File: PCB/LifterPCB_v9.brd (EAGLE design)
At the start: 64.9 x 58.5 mm, 8 parts

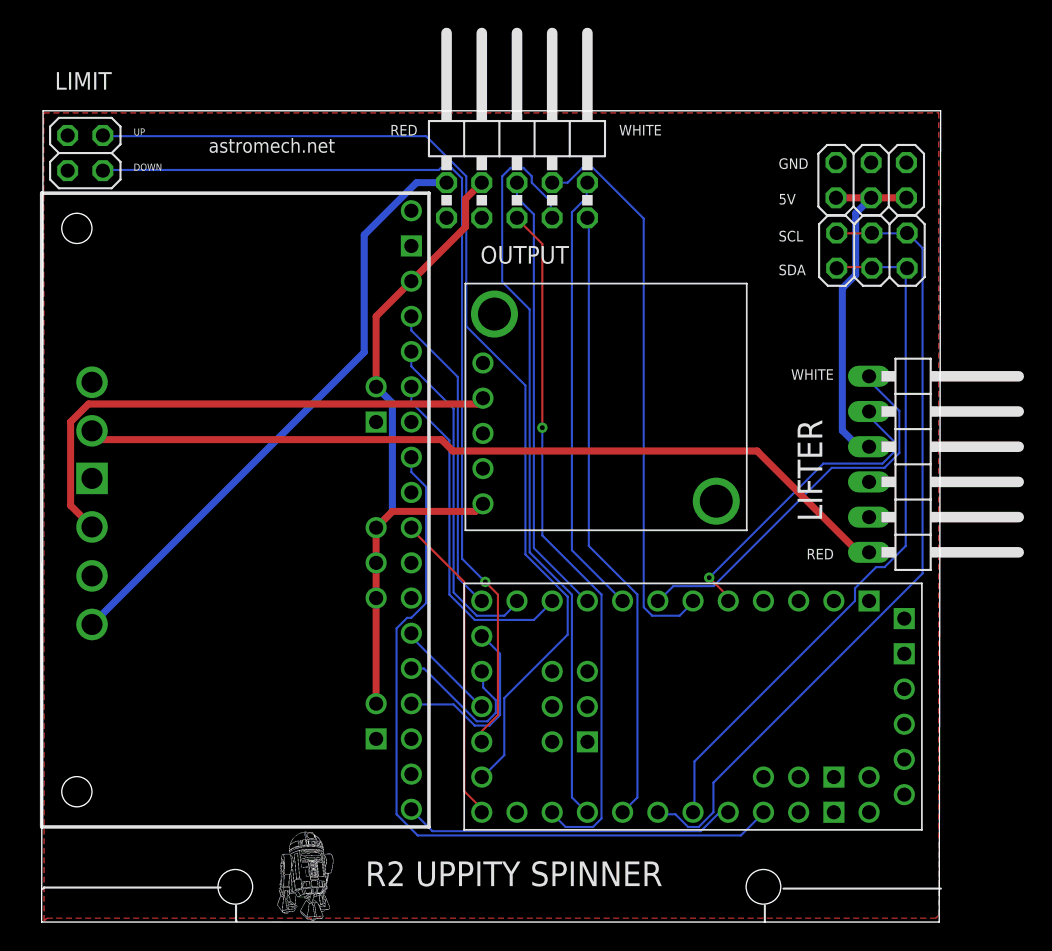
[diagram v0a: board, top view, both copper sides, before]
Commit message: Latest version of Eagle board files plus Eagle v9 version
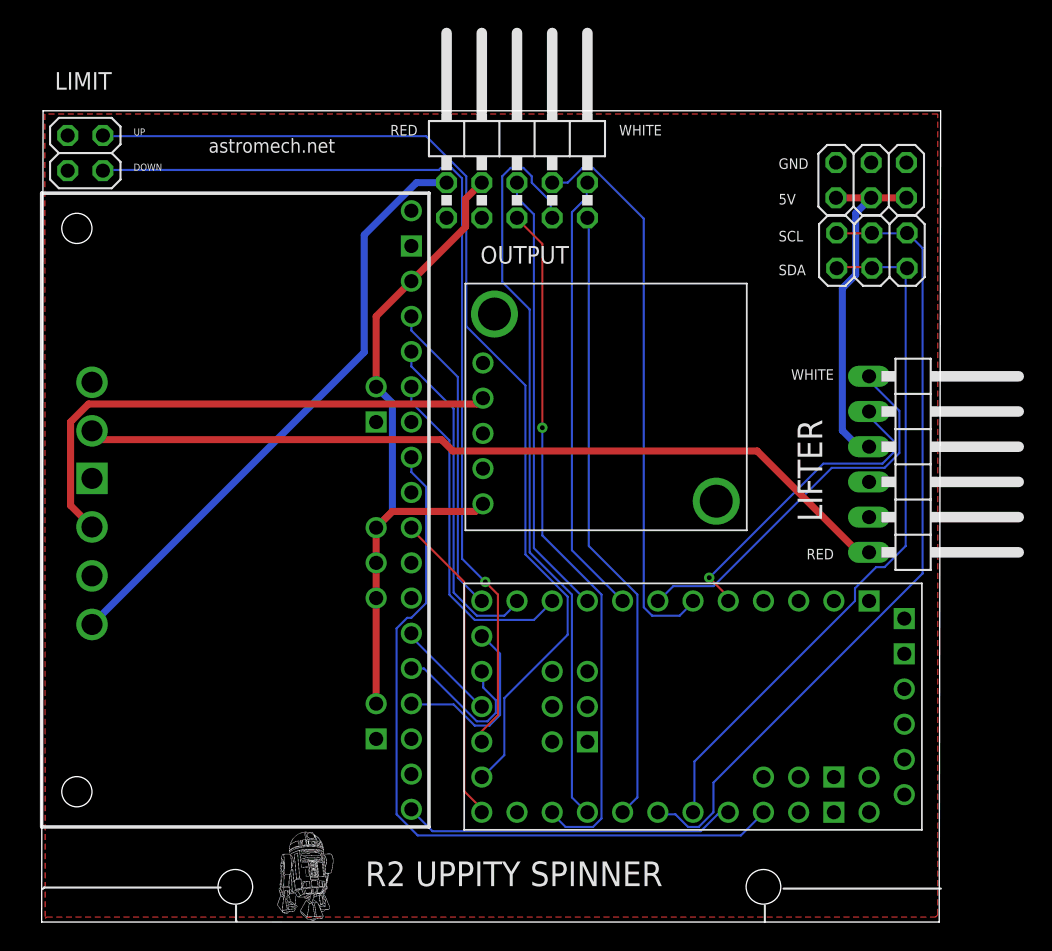
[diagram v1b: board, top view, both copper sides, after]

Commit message: This version uses thicker traces and adds a copper pour. The lifter board is a four layer board. The order of the connection pins on the rotary has changed. Do NOT use the same cable as the older board. The order was changed to allow using a silicone ribbon cable.
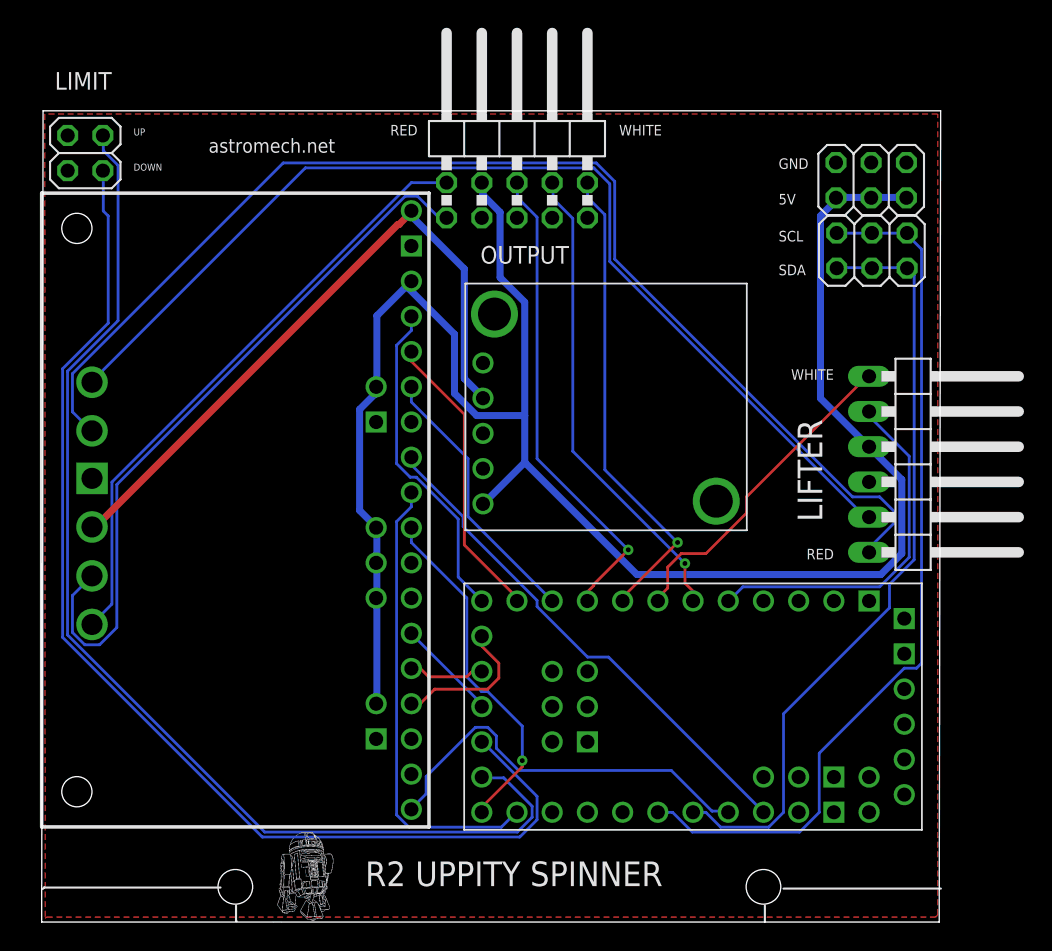
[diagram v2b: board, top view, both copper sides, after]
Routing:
- net +5V: track 101.3 -> 138.4 mm
- net LMOT2: track 59.7 -> 87.7 mm
- net M1SF: track 55.1 -> 37.0 mm
- net LMOT1: track 60.1 -> 76.2 mm
- net LFT_TOP: track 68.6 -> 83.2 mm, vias 1 -> 0
- net RMOT1: track 37.7 -> 52.1 mm
- net +12V: track 103.0 -> 90.5 mm
- net LKIT_B: track 54.7 -> 43.9 mm
- net M1FB: track 26.2 -> 33.2 mm
- net LFT_BOT: track 76.4 -> 83.1 mm
- net RTR_ENA: track 40.9 -> 34.5 mm, vias 0 -> 1
- net LKIT_A: track 50.2 -> 43.9 mm, vias 1 -> 0
- net M2IN1: track 11.3 -> 5.54 mm
- net M1PWM2: track 24.9 -> 19.7 mm
- net SDA: track 58.6 -> 63.7 mm
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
